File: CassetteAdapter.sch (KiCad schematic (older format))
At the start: 19 parts, among them CN1 AUDIO_IN, CN101 AUDIO_IN_JACK, CN2 TAPE_PORT, U1 CD4049, U2 LM741

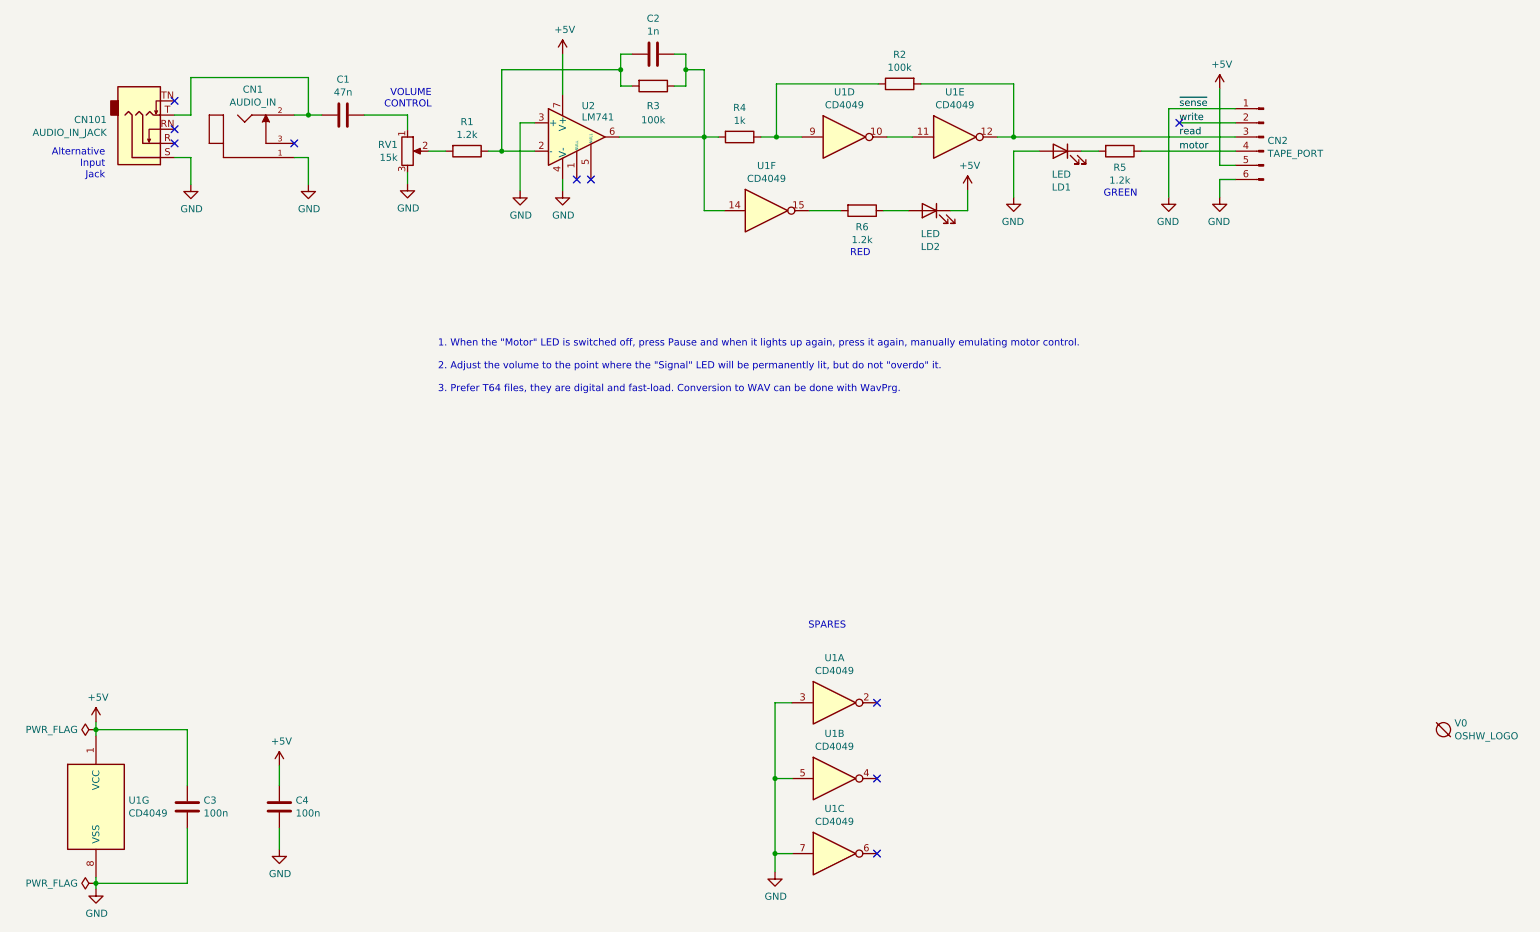
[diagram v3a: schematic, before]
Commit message: Add possibility to invert signal
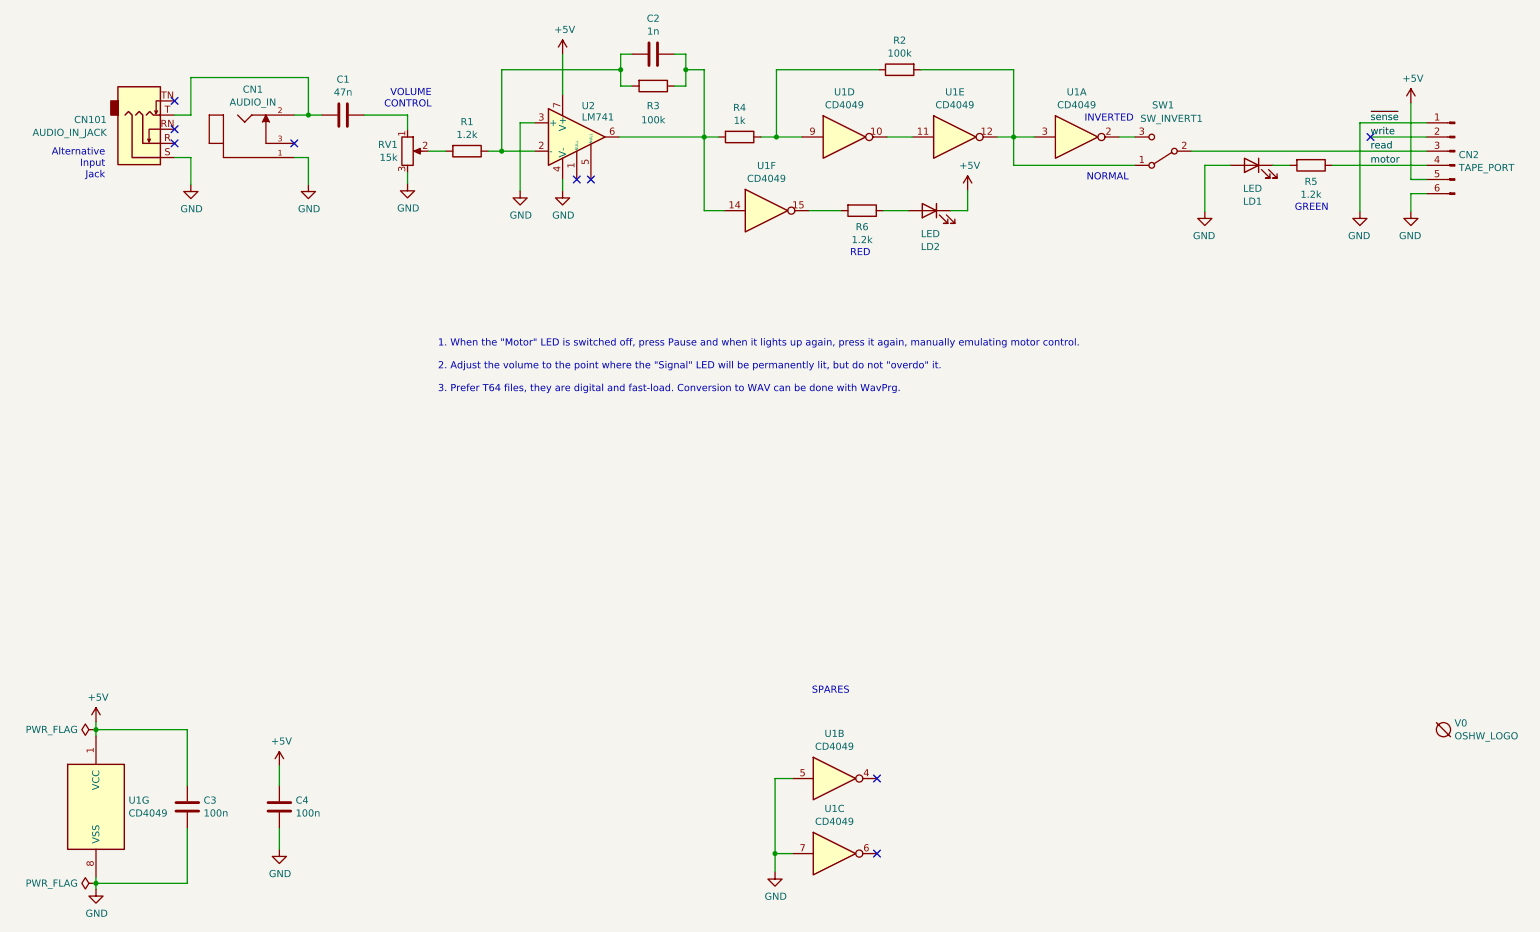
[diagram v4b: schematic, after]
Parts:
- added SW1: SW_INVERT1, Connector_PinHeader_2.54mm:PinHeader_1x03_P2.54mm_Vertical, symbol Switch:SW_SPDT
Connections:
- net GND: no longer U1.3
- net read: now also SW1.2 (B); no longer R2.2, U1.12
- net at U1.2: now also SW1.3 (C)
- new net: R2.2, SW1.1 (A), U1.12, U1.3
- no-connect marks 10 -> 9
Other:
- note added: "INVERTED"
- note added: "NORMAL"
- moved on the sheet: CN2, LD1, R2, R5, U1A
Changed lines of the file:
@@
 Sheet 1 1
 Title "Audio to Datassette Adapter"
-Date "2025-03-16"
+Date "2025-03-29"
 Rev "1git"
 Comp "SukkoPera"
@@
 L 4xxx:4049 U1
 U 1 1 67A8BB28
-P 6290 6190
-F 0 "U1" H 6290 6507 50  0000 C CNN
-F 1 "CD4049" H 6290 6416 50  0000 C CNN
-F 2 "Package_DIP:DIP-16_W7.62mm_Socket_LongPads" H 6290 6190 50  0001 C CNN
-F 3 "http://www.intersil.com/content/dam/intersil/documents/cd40/cd4049ubms.pdf" H 6290 6190 50  0001 C CNN
-	1    6290 6190
+P 8000 2195
+F 0 "U1" H 8000 2512 50  0000 C CNN
+F 1 "CD4049" H 8000 2421 50  0000 C CNN
+F 2 "Package_DIP:DIP-16_W7.62mm_Socket_LongPads" H 8000 2195 50  0001 C CNN
+F 3 "http://www.intersil.com/content/dam/intersil/documents/cd40/cd4049ubms.pdf" H 8000 2195 50  0001 C CNN
+	1    8000 2195
 	1    0    0    -1
 $EndComp
@@
 L Device:LED LD1
 U 1 1 67A91BED
-P 7885 2295
-F 0 "LD1" H 7878 2040 50  0000 C CNN
-F 1 "LED" H 7878 2131 50  0000 C CNN
-F 2 "LED_THT:LED_D3.0mm" H 7885 2295 50  0001 C CNN
-F 3 "~" H 7885 2295 50  0001 C CNN
-	1    7885 2295
+P 9235 2395
+F 0 "LD1" H 9228 2140 50  0000 C CNN
+F 1 "LED" H 9228 2231 50  0000 C CNN
+F 2 "LED_THT:LED_D3.0mm" H 9235 2395 50  0001 C CNN
+F 3 "~" H 9235 2395 50  0001 C CNN
+	1    9235 2395
 	-1   0    0    -1
 $EndComp
@@
 L Device:R R2
 U 1 1 67AA6305
-P 6750 1820
-F 0 "R2" V 6543 1820 50  0000 C CNN
-F 1 "100k" V 6634 1820 50  0000 C CNN
-F 2 "Resistor_THT:R_Axial_DIN0207_L6.3mm_D2.5mm_P10.16mm_Horizontal" V 6680 1820 50  0001 C CNN
-F 3 "~" H 6750 1820 50  0001 C CNN
-	1    6750 1820
+P 6750 1720
+F 0 "R2" V 6543 1720 50  0000 C CNN
+F 1 "100k" V 6634 1720 50  0000 C CNN
+F 2 "Resistor_THT:R_Axial_DIN0207_L6.3mm_D2.5mm_P10.16mm_Horizontal" V 6680 1720 50  0001 C CNN
+F 3 "~" H 6750 1720 50  0001 C CNN
+	1    6750 1720
 	0    -1   1    0
 $EndComp
@@
 	6660 2195 6840 2195
 Wire Wire Line
-	6600 1820 5880 1820
-Wire Wire Line
-	5880 2195 5880 1820
-Wire Wire Line
-	6900 1820 7555 1820
-Wire Wire Line
-	7555 1820 7555 2195
+	6600 1720 5880 1720
+Wire Wire Line
+	5880 2195 5880 1720
+Wire Wire Line
+	6900 1720 7555 1720
+Wire Wire Line
+	7555 1720 7555 2195
 Wire Wire Line
 	7555 2195 7440 2195
@@
 L Connector:Conn_01x06_Male J?
 U 1 1 67ACD4FD
-P 9320 2195
+P 10670 2295
 AR Path="/67ABBA81/67ACD4FD" Ref="J?"  Part="1"
 AR Path="/67ACD4FD" Ref="CN2"  Part="1"
-F 0 "CN2" H 9292 2169 50  0000 R CNN
-F 1 "TAPE_PORT" H 9292 2078 50  0000 R CNN
-F 2 "CassetteAdapter:C64-Cassette-Port-Female" H 9320 2195 50  0001 C CNN
-F 3 "~" H 9320 2195 50  0001 C CNN
-	1    9320 2195
+F 0 "CN2" H 10642 2269 50  0000 R CNN
+F 1 "TAPE_PORT" H 10642 2178 50  0000 R CNN
+F 2 "CassetteAdapter:C64-Cassette-Port-Female" H 10670 2295 50  0001 C CNN
+F 3 "~" H 10670 2295 50  0001 C CNN
+	1    10670 2295
 	-1   0    0    -1
 $EndComp
 Wire Wire Line
-	9120 2395 9010 2395
-Wire Wire Line
-	9010 2395 9010 1855
-Wire Wire Line
-	9120 2495 9010 2495
-Wire Wire Line
-	9010 2495 9010 2620
+	10470 2495 10360 2495
+Wire Wire Line
+	10360 2495 10360 1955
+Wire Wire Line
+	10470 2595 10360 2595
+Wire Wire Line
+	10360 2595 10360 2720
 $Comp
 L power:GND #PWR?
 U 1 1 67ACD507
-P 9010 2620
+P 10360 2720
 AR Path="/67ABBA81/67ACD507" Ref="#PWR?"  Part="1"
 AR Path="/67ACD507" Ref="#PWR011"  Part="1"
-F 0 "#PWR011" H 9010 2370 50  0001 C CNN
-F 1 "GND" H 9015 2447 50  0000 C CNN
-F 2 "" H 9010 2620 50  0001 C CNN
-F 3 "" H 9010 2620 50  0001 C CNN
-	1    9010 2620
+F 0 "#PWR011" H 10360 2470 50  0001 C CNN
+F 1 "GND" H 10365 2547 50  0000 C CNN
+F 2 "" H 10360 2720 50  0001 C CNN
+F 3 "" H 10360 2720 50  0001 C CNN
+	1    10360 2720
 	-1   0    0    -1
 $EndComp
 Wire Wire Line
-	9120 2095 8725 2095
-Text Label 8725 1995 0    50   ~ 0
+	10470 2195 10075 2195
+Text Label 10075 2095 0    50   ~ 0
 ~sense
-Text Label 8725 2095 0    50   ~ 0
+Text Label 10075 2195 0    50   ~ 0
 write
-Text Label 8725 2195 0    50   ~ 0
+Text Label 10075 2295 0    50   ~ 0
 read
-Text Label 8725 2295 0    50   ~ 0
+Text Label 10075 2395 0    50   ~ 0
 motor
 $Comp
 L power:+5V #PWR?
 U 1 1 67ACD515
-P 9010 1855
+P 10360 1955
 AR Path="/67ABBA81/67ACD515" Ref="#PWR?"  Part="1"
 AR Path="/67ACD515" Ref="#PWR07"  Part="1"
-F 0 "#PWR07" H 9010 1705 50  0001 C CNN
-F 1 "+5V" H 9025 2028 50  0000 C CNN
-F 2 "" H 9010 1855 50  0001 C CNN
-F 3 "" H 9010 1855 50  0001 C CNN
-	1    9010 1855
-	1    0    0    -1
-$EndComp
-Wire Wire Line
-	7555 2195 9120 2195
-NoConn ~ 8725 2095
-Wire Wire Line
-	8650 1995 8650 2620
-Wire Wire Line
-	8650 1995 9120 1995
+F 0 "#PWR07" H 10360 1805 50  0001 C CNN
+F 1 "+5V" H 10375 2128 50  0000 C CNN
+F 2 "" H 10360 1955 50  0001 C CNN
+F 3 "" H 10360 1955 50  0001 C CNN
+	1    10360 1955
+	1    0    0    -1
+$EndComp
+Wire Wire Line
+	7555 2195 7700 2195
+NoConn ~ 10075 2195
+Wire Wire Line
+	10000 2095 10000 2720
+Wire Wire Line
+	10000 2095 10470 2095
 $Comp
 L power:GND #PWR?
 U 1 1 67AD08F2
-P 8650 2620
+P 10000 2720
 AR Path="/67ABBA81/67AD08F2" Ref="#PWR?"  Part="1"
 AR Path="/67AD08F2" Ref="#PWR010"  Part="1"
-F 0 "#PWR010" H 8650 2370 50  0001 C CNN
-F 1 "GND" H 8655 2447 50  0000 C CNN
-F 2 "" H 8650 2620 50  0001 C CNN
-F 3 "" H 8650 2620 50  0001 C CNN
-	1    8650 2620
+F 0 "#PWR010" H 10000 2470 50  0001 C CNN
+F 1 "GND" H 10005 2547 50  0000 C CNN
+F 2 "" H 10000 2720 50  0001 C CNN
+F 3 "" H 10000 2720 50  0001 C CNN
+	1    10000 2720
 	-1   0    0    -1
 $EndComp
@@
 L Device:R R5
 U 1 1 67B0E4F9
-P 8305 2295
-F 0 "R5" V 8420 2295 50  0000 C CNN
-F 1 "1.2k" V 8511 2295 50  0000 C CNN
-F 2 "Resistor_THT:R_Axial_DIN0207_L6.3mm_D2.5mm_P10.16mm_Horizontal" V 8235 2295 50  0001 C CNN
-F 3 "~" H 8305 2295 50  0001 C CNN
-	1    8305 2295
+P 9655 2395
+F 0 "R5" V 9770 2395 50  0000 C CNN
+F 1 "1.2k" V 9861 2395 50  0000 C CNN
+F 2 "Resistor_THT:R_Axial_DIN0207_L6.3mm_D2.5mm_P10.16mm_Horizontal" V 9585 2395 50  0001 C CNN
+F 3 "~" H 9655 2395 50  0001 C CNN
+	1    9655 2395
 	0    1    1    0
 $EndComp
 Wire Wire Line
-	8455 2295 9120 2295
-Wire Wire Line
-	8035 2295 8155 2295
+	9805 2395 10470 2395
+Wire Wire Line
+	9385 2395 9505 2395
 Wire Wire Line
 	7230 2715 7230 2570
@@
 $EndComp
 Wire Wire Line
-	7735 2295 7555 2295
-Wire Wire Line
-	7555 2295 7555 2620
+	9085 2395 8905 2395
+Wire Wire Line
+	8905 2395 8905 2720
 $Comp
 L power:GND #PWR?
 U 1 1 67B1AED0
-P 7555 2620
+P 8905 2720
 AR Path="/67ABBA81/67B1AED0" Ref="#PWR?"  Part="1"
 AR Path="/67B1AED0" Ref="#PWR09"  Part="1"
-F 0 "#PWR09" H 7555 2370 50  0001 C CNN
-F 1 "GND" H 7560 2447 50  0000 C CNN
-F 2 "" H 7555 2620 50  0001 C CNN
-F 3 "" H 7555 2620 50  0001 C CNN
-	1    7555 2620
+F 0 "#PWR09" H 8905 2470 50  0001 C CNN
+F 1 "GND" H 8910 2547 50  0000 C CNN
+F 2 "" H 8905 2720 50  0001 C CNN
+F 3 "" H 8905 2720 50  0001 C CNN
+	1    8905 2720
 	-1   0    0    -1
 $EndComp
-Wire Wire Line
-	5990 6190 5870 6190
-Wire Wire Line
-	5870 6190 5870 6725
 $Comp
 L power:GND #PWR0101
@@
 Wire Wire Line
 	5990 6725 5870 6725
-Connection ~ 5870 6725
 Wire Wire Line
 	5870 6725 5870 7255
 NoConn ~ 6590 7255
 NoConn ~ 6590 6725
-NoConn ~ 6590 6190
-Text Notes 6105 5675 0    50   ~ 0
+Text Notes 6130 6135 0    50   ~ 0
 SPARES
 Wire Wire Line
@@
 Text Notes 6400 3045 0    50   ~ 0
 RED
-Text Notes 8190 2625 0    50   ~ 0
+Text Notes 9540 2725 0    50   ~ 0
 GREEN
 $Comp
@@
 	1    0    0    -1
 $EndComp
+Wire Wire Line
+	8300 2195 8410 2195
+$Comp
+L Switch:SW_SPDT SW1
+U 1 1 67E913EF
+P 8610 2295
+F 0 "SW1" H 8610 1970 50  0000 C CNN
+F 1 "SW_INVERT1" H 8550 2065 50  0000 C CNN
+F 2 "Connector_PinHeader_2.54mm:PinHeader_1x03_P2.54mm_Vertical" H 8610 2295 50  0001 C CNN
+F 3 "~" H 8610 2295 50  0001 C CNN
+	1    8610 2295
+	-1   0    0    1
+$EndComp
+Wire Wire Line
+	7555 2195 7555 2395
+Wire Wire Line
+	7555 2395 8410 2395
+Text Notes 8070 2510 0    50   ~ 0
+NORMAL
+Wire Wire Line
+	8810 2295 10470 2295
+Text Notes 8055 2095 0    50   ~ 0
+INVERTED
 $EndSCHEMATC

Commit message: Fix LEDs
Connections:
- net +5V: now also LD2.2 (A); no longer LD2.1 (K)
- net GND: now also LD1.1 (K); no longer LD1.2 (A)
- net at R6.1: now also LD2.1 (K); no longer LD2.2 (A)
- net at R5.2: now also LD1.2 (A); no longer LD1.1 (K)
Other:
- moved on the sheet: LD1, LD2
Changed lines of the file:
@@
 F 3 "~" H 6960 2715 50  0001 C CNN
 	1    6960 2715
-	-1   0    0    -1
+	1    0    0    -1
 $EndComp
 $Comp
@@
 U 1 1 67A91BED
 P 9235 2395
-F 0 "LD1" H 9228 2140 50  0000 C CNN
-F 1 "LED" H 9228 2231 50  0000 C CNN
+F 0 "LD1" H 9228 2232 50  0000 C CNN
+F 1 "LED" H 9228 2141 50  0000 C CNN
 F 2 "LED_THT:LED_D3.0mm" H 9235 2395 50  0001 C CNN
 F 3 "~" H 9235 2395 50  0001 C CNN
 	1    9235 2395
-	-1   0    0    -1
+	1    0    0    -1
 $EndComp
 Wire Wire Line
@@
 	9385 2395 9505 2395
 Wire Wire Line
-	7230 2715 7230 2570
-$Comp
-L power:+5V #PWR?
-U 1 1 67B18F86
-P 7230 2570
-AR Path="/67ABBA81/67B18F86" Ref="#PWR?"  Part="1"
-AR Path="/67B18F86" Ref="#PWR08"  Part="1"
-F 0 "#PWR08" H 7230 2420 50  0001 C CNN
-F 1 "+5V" H 7245 2743 50  0000 C CNN
-F 2 "" H 7230 2570 50  0001 C CNN
-F 3 "" H 7230 2570 50  0001 C CNN
-	1    7230 2570
-	1    0    0    -1
-$EndComp
-Wire Wire Line
 	9085 2395 8905 2395
 Wire Wire Line
@@
 Text Notes 8055 2095 0    50   ~ 0
 INVERTED
+Wire Wire Line
+	7230 2715 7230 2595
+$Comp
+L power:+5V #PWR?
+U 1 1 67EA1CDE
+P 7230 2595
+AR Path="/67ABBA81/67EA1CDE" Ref="#PWR?"  Part="1"
+AR Path="/67EA1CDE" Ref="#PWR?"  Part="1"
+F 0 "#PWR?" H 7230 2445 50  0001 C CNN
+F 1 "+5V" H 7245 2768 50  0000 C CNN
+F 2 "" H 7230 2595 50  0001 C CNN
+F 3 "" H 7230 2595 50  0001 C CNN
+	1    7230 2595
+	1    0    0    -1
+$EndComp
 $EndSCHEMATC

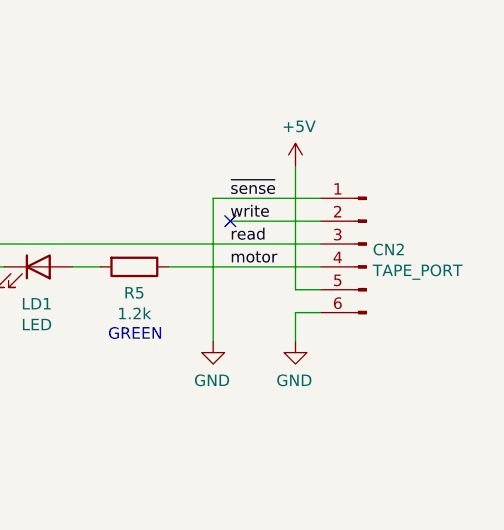
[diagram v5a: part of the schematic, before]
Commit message: Fix edge connector orientation, sigh...
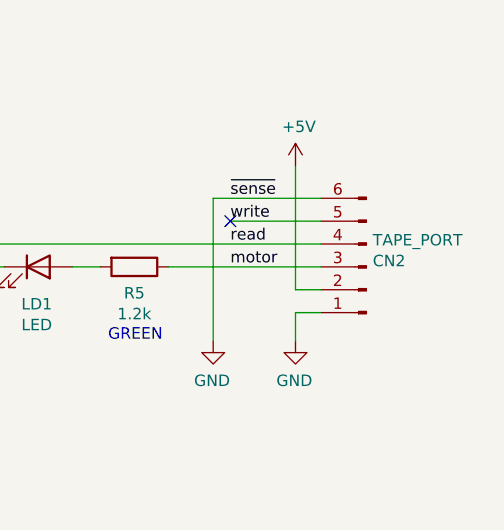
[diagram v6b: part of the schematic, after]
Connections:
- net +5V: now also CN2.2 (Pin_2); no longer CN2.5 (Pin_5)
- net motor: now also CN2.3 (Pin_3); no longer CN2.4 (Pin_4)
- net read: now also CN2.4 (Pin_4); no longer CN2.3 (Pin_3)
- net write: now also CN2.5 (Pin_5); no longer CN2.2 (Pin_2)
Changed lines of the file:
@@
 Sheet 1 1
 Title "Audio to Datassette Adapter"
-Date "2025-03-29"
+Date "2025-05-21"
 Rev "1git"
 Comp "SukkoPera"
@@
 	7555 2195 7440 2195
 Connection ~ 7555 2195
-$Comp
-L Connector:Conn_01x06_Male J?
-U 1 1 67ACD4FD
-P 10670 2295
-AR Path="/67ABBA81/67ACD4FD" Ref="J?"  Part="1"
-AR Path="/67ACD4FD" Ref="CN2"  Part="1"
-F 0 "CN2" H 10642 2269 50  0000 R CNN
-F 1 "TAPE_PORT" H 10642 2178 50  0000 R CNN
-F 2 "CassetteAdapter:C64-Cassette-Port-Female" H 10670 2295 50  0001 C CNN
-F 3 "~" H 10670 2295 50  0001 C CNN
-	1    10670 2295
-	-1   0    0    -1
-$EndComp
 Wire Wire Line
 	10470 2495 10360 2495
@@
 	1    0    0    -1
 $EndComp
+$Comp
+L Connector:Conn_01x06_Male J?
+U 1 1 67ACD4FD
+P 10670 2395
+AR Path="/67ABBA81/67ACD4FD" Ref="J?"  Part="1"
+AR Path="/67ACD4FD" Ref="CN2"  Part="1"
+F 0 "CN2" H 10642 2369 50  0000 R CNN
+F 1 "TAPE_PORT" H 10642 2278 50  0000 R CNN
+F 2 "CassetteAdapter:C64-Cassette-Port-Female" H 10670 2395 50  0001 C CNN
+F 3 "~" H 10670 2395 50  0001 C CNN
+	1    10670 2395
+	-1   0    0    1
+$EndComp
 $EndSCHEMATC

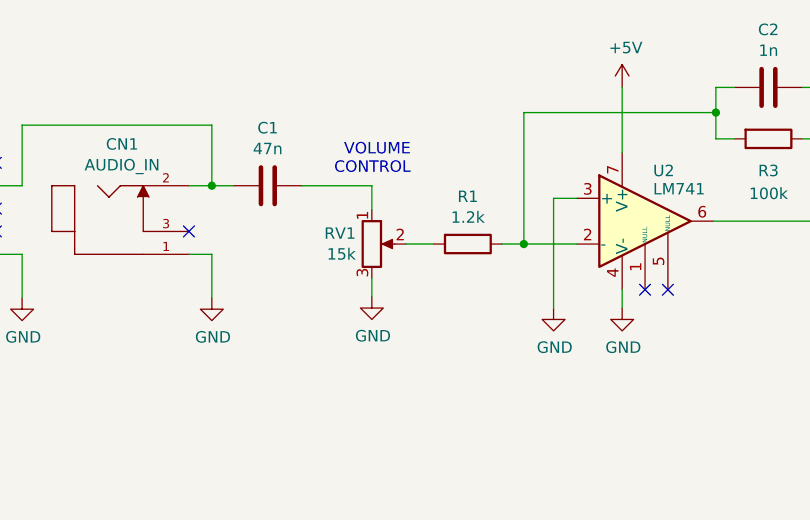
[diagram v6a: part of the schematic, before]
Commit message: More common component values
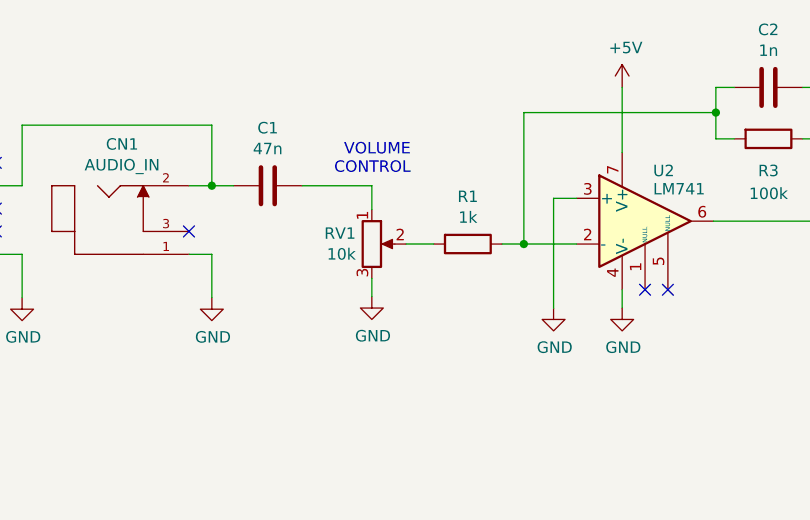
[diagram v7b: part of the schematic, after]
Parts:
- R1: value 1.2k -> 1k
- RV1: value 15k -> 10k
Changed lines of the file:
@@
 P 3695 2295
 F 0 "R1" V 3488 2295 50  0000 C CNN
-F 1 "1.2k" V 3579 2295 50  0000 C CNN
+F 1 "1k" V 3579 2295 50  0000 C CNN
 F 2 "Resistor_THT:R_Axial_DIN0207_L6.3mm_D2.5mm_P10.16mm_Horizontal" V 3625 2295 50  0001 C CNN
 F 3 "~" H 3695 2295 50  0001 C CNN
@@
 P 3275 2295
 F 0 "RV1" H 3205 2341 50  0000 R CNN
-F 1 "15k" H 3205 2250 50  0000 R CNN
+F 1 "10k" H 3205 2250 50  0000 R CNN
 F 2 "CassetteAdapter:Pot_Bourns_3306P" H 3275 2295 50  0001 C CNN
 F 3 "~" H 3275 2295 50  0001 C CNN
